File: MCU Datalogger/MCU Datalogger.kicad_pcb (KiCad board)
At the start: 2 copper layers, 50.8 x 30.5 mm, 30 parts, among them J1 Conn_01x04_Pin, J2 Conn_01x09_Pin, J3 Conn_01x04_Pin, J4 Conn_02x03_Odd_Even, U1 24LC1025, U2 DS1337S_, U3 24LC1025, U4 ATMEGA328P-AU, Y1 32.768KHz, Y2 16MHz

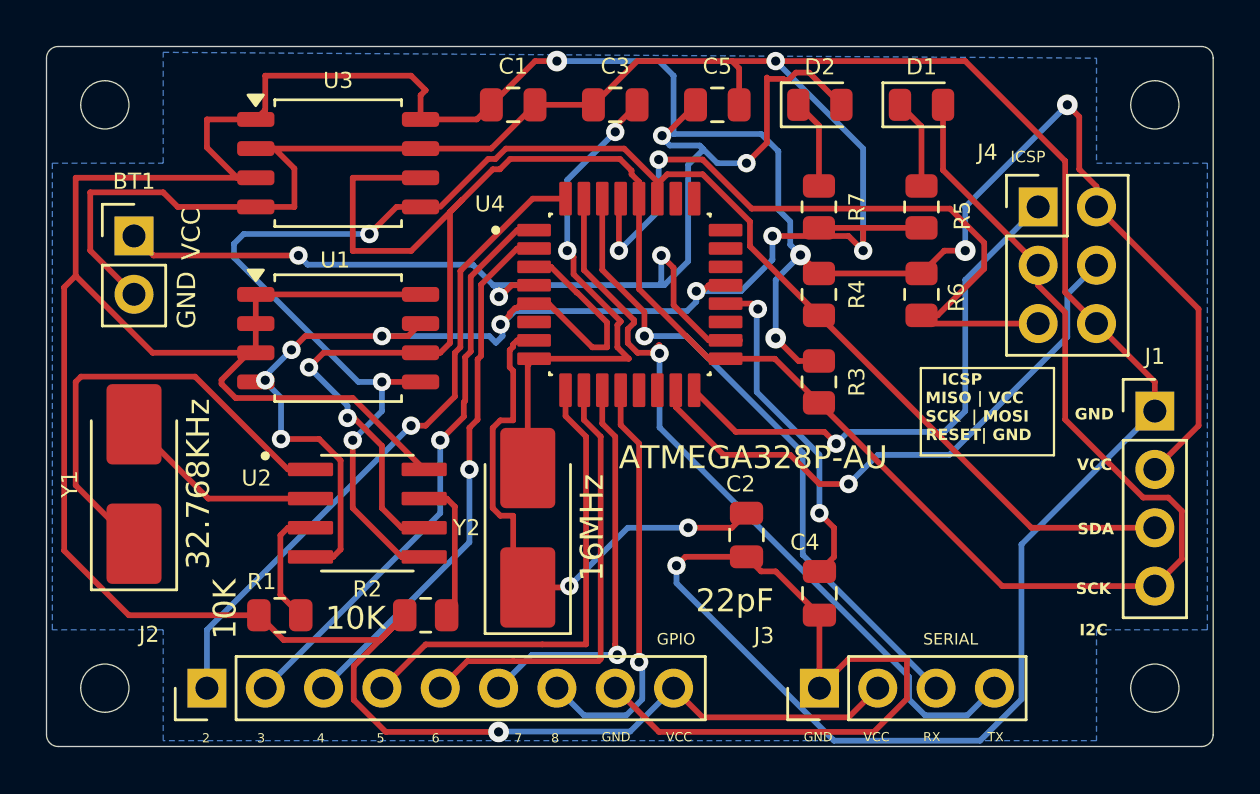
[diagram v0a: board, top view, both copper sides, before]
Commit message: main: updated schematic due to SCL and SCK mixup
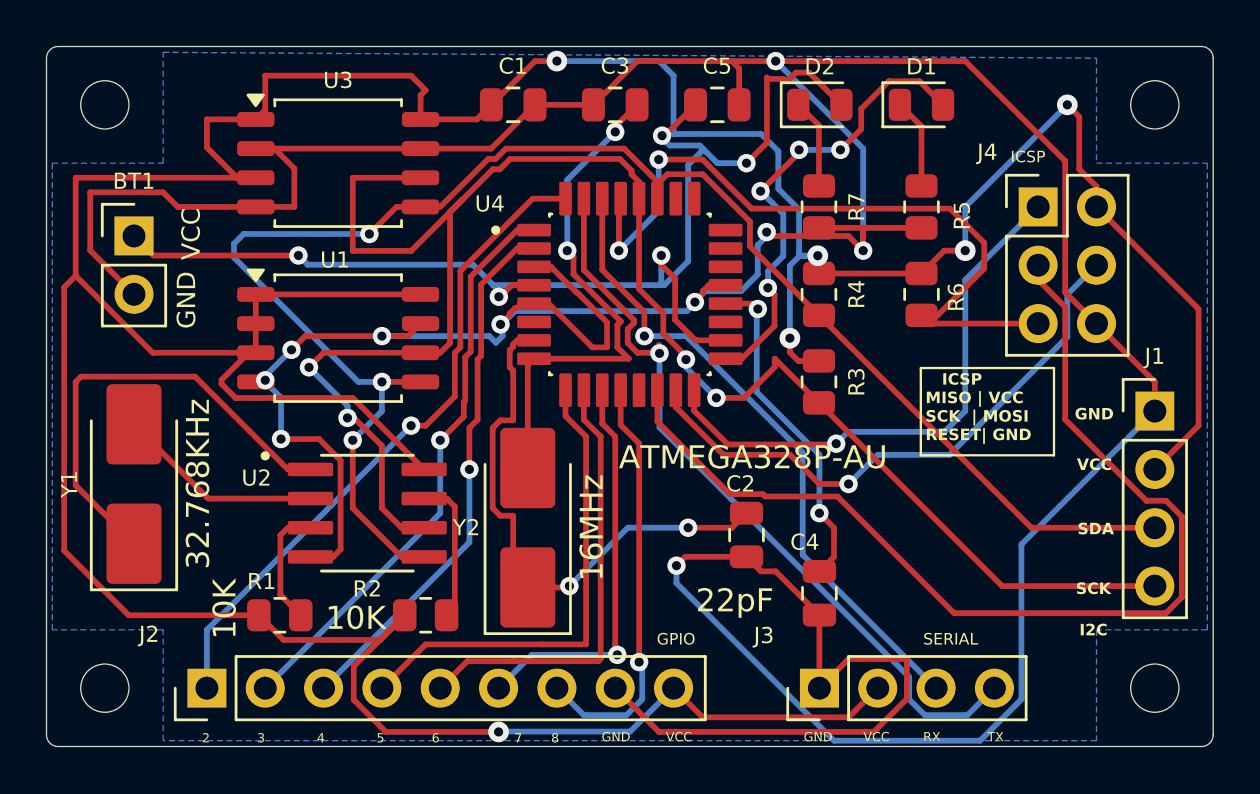
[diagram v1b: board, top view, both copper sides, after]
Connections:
- D1 pad 2: /SCK -> /D9
- J1 pad 4: /SCK -> /SCL
- R3 pad 2: /SCK -> /SCL
- U1 pad 6: /SCK -> /SCL
- U2 pad 6: /SCK -> /SCL
- U3 pad 6: /SCK -> /SCL
- U4 pad 14: unconnected-(U4-PB2-Pad14) -> /SCK
- U4 pad 17: /SCK -> /D9
- U4 pad 28: /SCK -> /SCL
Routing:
- net /SCL: track 0.00 -> 78.5 mm, vias 0 -> 4
- net /SCK: track 102.5 -> 45.5 mm, vias 2 -> 0
- net /D9: track 0.00 -> 20.3 mm, vias 0 -> 4
- net /Vcc: track 240.0 -> 240.9 mm
- net /MISO: track 23.6 -> 24.1 mm
- net GND: track 208.0 -> 208.5 mm
